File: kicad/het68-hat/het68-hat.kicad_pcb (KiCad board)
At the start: 2 copper layers, 94 x 96 mm, 91 parts, among them J1 MIC1, J10 PWR, J11 PZ1, J12 PZ2, J13 PZ3, J14 PZ4, J17 UART, J2 MIC2, J3 MIC3, J4 MIC4, J5 MIC5, J6 MIC6, U1 Pico_Plus_2, U2 SN74LVC8T245, U3 SN74LVC8T245, U4 SN74LVC8T245, U5 AP2112K-1.8, U6 DRV8837C, U7 DPS310, U8 SHT40, U9 INA3221

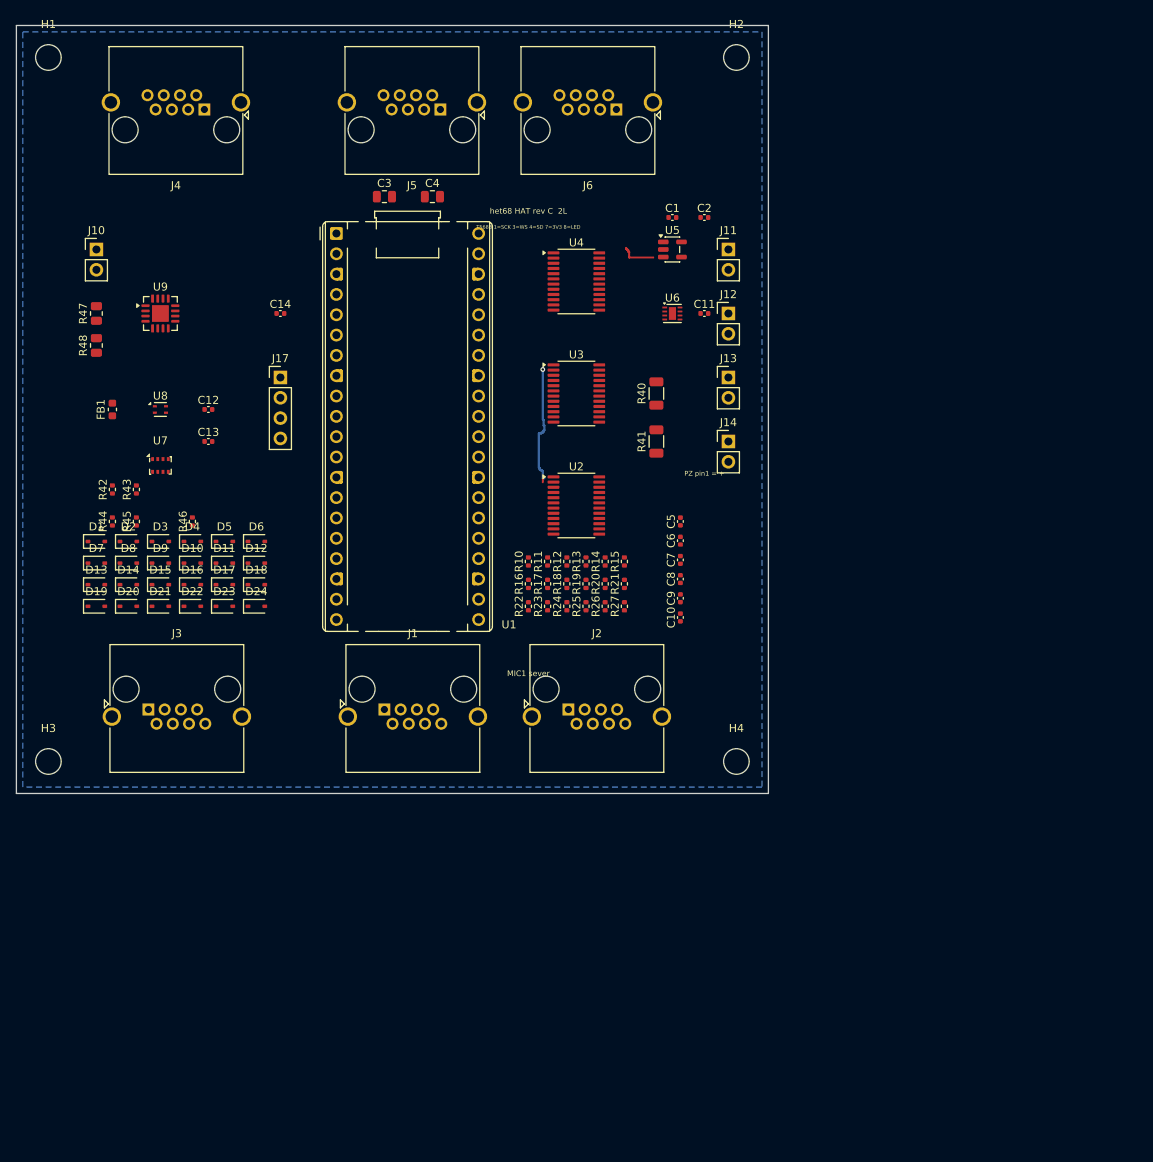
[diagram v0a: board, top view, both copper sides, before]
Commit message: Ship a four-layer HAT that is fully routed and ready to fab.
GPIO for SD and LED move to the jack rows so firmware can follow PINOUT.csv; power and satellite boards stay as in v1.10.0.

Co-authored-by: Cursor <cursoragent@cursor.com>
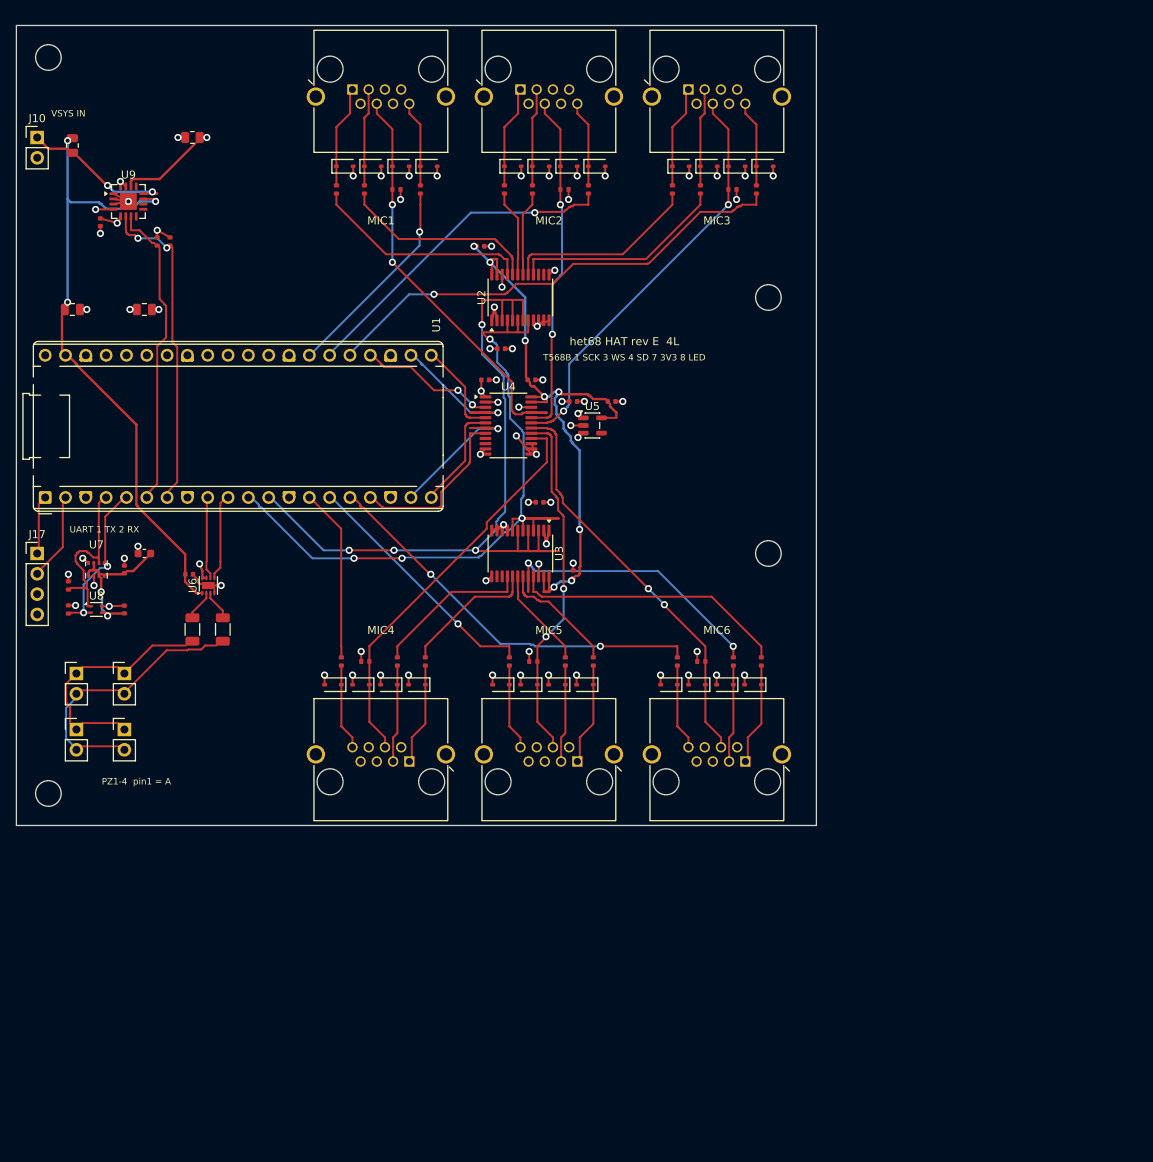
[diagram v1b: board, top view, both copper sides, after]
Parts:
- removed R46: 10k, R_0402_1005Metric
- added R50: 100k, Resistor_SMD:R_0402_1005Metric, F.Cu at (47.5, 20.5)
- added R51: 100k, Resistor_SMD:R_0402_1005Metric, F.Cu at (68.5, 20.5)
- added R52: 100k, Resistor_SMD:R_0402_1005Metric, F.Cu at (89.5, 20.5)
- added R53: 100k, Resistor_SMD:R_0402_1005Metric, F.Cu at (43.6, 79.5)
- added R54: 100k, Resistor_SMD:R_0402_1005Metric, F.Cu at (64.6, 79.5)
- added R55: 100k, Resistor_SMD:R_0402_1005Metric, F.Cu at (85.6, 79.5)
- C1, C10, C11, C12, C13, C14, C2, C5, C6, C7, C8, C9: footprint C_0402_1005Metric -> Capacitor_SMD:C_0402_1005Metric
- C3, C4: footprint C_0805_2012Metric -> Capacitor_SMD:C_0805_2012Metric
- D1, D10, D11, D12, D13, D14, D15, D16, D17, D18, D19, D2, D20, D21, D22, D23, D24, D3, D4, D5, D6, D7, D8, D9: footprint D_SOD-323 -> Diode_SMD:D_SOD-323
- FB1: footprint L_0603_1608Metric -> Inductor_SMD:L_0603_1608Metric
- H1, H2, H3, H4: footprint MountingHole_3.2mm_M3 -> MountingHole:MountingHole_3.2mm_M3
- J1, J2, J3, J4, J5, J6: footprint RJ45_Amphenol_RJHSE5380 -> het68:RJ45_RJHSE5380_het68
- J10, J11, J12, J13, J14: footprint PinHeader_1x02_P2.54mm_Vertical -> Connector_PinHeader_2.54mm:PinHeader_1x02_P2.54mm_Vertical
- J17: footprint PinHeader_1x04_P2.54mm_Vertical -> Connector_PinHeader_2.54mm:PinHeader_1x04_P2.54mm_Vertical
- R10, R11, R12, R13, R14, R15, R16, R17, R18, R19, R20, R21, R22, R23, R24, R25, R26, R27, R42, R43, R44, R45: footprint R_0402_1005Metric -> Resistor_SMD:R_0402_1005Metric
- R40, R41: footprint R_1206_3216Metric -> Resistor_SMD:R_1206_3216Metric
- R47, R48: footprint R_0805_2012Metric -> Resistor_SMD:R_0805_2012Metric
- U1: footprint RaspberryPi_Pico_Common_THT -> Module:RaspberryPi_Pico_Common_THT
- U2, U3, U4: footprint TSSOP-24_4.4x7.8mm_P0.65mm -> Package_SO:TSSOP-24_4.4x7.8mm_P0.65mm
- U5: footprint SOT-23-5 -> Package_TO_SOT_SMD:SOT-23-5
- U6: footprint Texas_DSG0008A_WSON-8-1EP_2x2mm_P0.5mm_EP0.9x1.6mm -> Package_SON:Texas_DSG0008A_WSON-8-1EP_2x2mm_P0.5mm_EP0.9x1.6mm
- U7: footprint Bosch_LGA-8_2x2.5mm_P0.65mm_ClockwisePinNumbering -> Package_LGA:Bosch_LGA-8_2x2.5mm_P0.65mm_ClockwisePinNumbering
- U8: footprint Sensirion_DFN-4_1.5x1.5mm_P0.8mm_SHT4x_NoCentralPad -> Sensor_Humidity:Sensirion_DFN-4_1.5x1.5mm_P0.8mm_SHT4x_NoCentralPad
- U9: footprint Texas_RGV0016A_VQFN-16-1EP_4x4mm_P0.65mm_EP2.1x2.1mm -> Package_DFN_QFN:Texas_RGV0016A_VQFN-16-1EP_4x4mm_P0.65mm_EP2.1x2.1mm
- moved H2 125.9 mm to (4.00, 96.0)
- moved H3 107.1 mm to (94.0, 34.0)
- moved J3 102.8 mm to (84.0, 8.00)
- moved J11 97.2 mm to (7.50, 81.0)
- moved J12 96.7 mm to (7.50, 88.0)
- moved J4 85.4 mm to (49.1, 92.0)
- moved J13 84.1 mm to (13.5, 81.0)
- moved J14 83.6 mm to (13.5, 88.0)
- moved J5 83.3 mm to (70.1, 92.0)
- moved J6 83.1 mm to (91.1, 92.0)
- moved D9 81.8 mm to (83.0, 17.6)
- moved D10 81.4 mm to (86.5, 17.6)
- moved D11 81.0 mm to (90.0, 17.6)
- moved D12 80.6 mm to (93.5, 17.6)
- moved J2 77.7 mm to (63.0, 8.00)
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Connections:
- U1 pad 14: LED1_G -> LED4_G
- U1 pad 15: LED2_G -> LED5_G
- U1 pad 16: LED3_G -> LED6_G
- U1 pad 17: LED4_G -> SD4_3V3
- U1 pad 19: LED5_G -> SD5_3V3
- U1 pad 20: (no net) -> SD6_3V3
- U1 pad 21: SD1_3V3 -> SD3_3V3
- U1 pad 22: (no net) -> SD2_3V3
- U1 pad 24: SD2_3V3 -> SD1_3V3
- U1 pad 25: (no net) -> LED3_G
- U1 pad 26: SD3_3V3 -> LED2_G
- U1 pad 27: (no net) -> LED1_G
- U1 pad 29: LED6_G -> unconnected-(U1-GP22-Pad29)
- U1 pad 30: RUN -> unconnected-(U1-RUN-Pad30)
- U1 pad 31: SD4_3V3 -> unconnected-(U1-GP26-Pad31)
- U1 pad 32: SD5_3V3 -> unconnected-(U1-GP27-Pad32)
- U1 pad 34: SD6_3V3 -> unconnected-(U1-GP28-Pad34)
- U1 pad 35: +3V3 -> unconnected-(U1-ADC_VREF-Pad35)
- U1 pad 37: (no net) -> unconnected-(U1-3V3_EN-Pad37)
- U1 pad 40: (no net) -> unconnected-(U1-VBUS-Pad40)
- U2 pad 14: (no net) -> unconnected-(U2-B8-Pad14)
- U2 pad 15: (no net) -> unconnected-(U2-B7-Pad15)
- U2 pad 16: SCK6_B -> WS3_B
- U2 pad 17: SCK5_B -> SCK3_B
- U2 pad 18: SCK4_B -> WS2_B
- U2 pad 19: SCK3_B -> SCK2_B
- U2 pad 20: SCK2_B -> WS1_B
- U2 pad 4: SCK_3V3 -> WS_3V3
- U2 pad 6: SCK_3V3 -> WS_3V3
- U2 pad 8: SCK_3V3 -> WS_3V3
- U3 pad 14: (no net) -> unconnected-(U3-B8-Pad14)
- U3 pad 15: (no net) -> unconnected-(U3-B7-Pad15)
- U3 pad 16: WS6_B -> WS4_B
- U3 pad 17: WS5_B -> SCK4_B
- U3 pad 18: WS4_B -> WS5_B
- U3 pad 19: WS3_B -> SCK5_B
- U3 pad 20: WS2_B -> WS6_B
- U3 pad 21: WS1_B -> SCK6_B
- U3 pad 3: WS_3V3 -> SCK_3V3
- U3 pad 5: WS_3V3 -> SCK_3V3
- U3 pad 7: WS_3V3 -> SCK_3V3
- U4 pad 10: (no net) -> unconnected-(U4-A8-Pad10)
- U4 pad 16: SD6_18 -> SD4_18
- U4 pad 18: SD4_18 -> SD6_18
- U4 pad 6: SD4_3V3 -> SD6_3V3
- U4 pad 8: SD6_3V3 -> SD4_3V3
- U4 pad 9: (no net) -> unconnected-(U4-A7-Pad9)
- U5 pad 4: (no net) -> unconnected-(U5-NC-Pad4)
- U9 pad 10: (no net) -> unconnected-(U9-PV-Pad10)
- U9 pad 13: (no net) -> unconnected-(U9-TC-Pad13)
- U9 pad 8: (no net) -> unconnected-(U9-WARNING-Pad8)
- U9 pad 9: (no net) -> unconnected-(U9-CRITICAL-Pad9)
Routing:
- net SCK_3V3: track 0.00 -> 98.5 mm, vias 0 -> 4
- net WS_3V3: track 0.00 -> 90.1 mm, vias 0 -> 4
- net GND: track 0.00 -> 89.3 mm, vias 0 -> 59
- net +1V8: track 0.00 -> 79.0 mm, vias 0 -> 8
- net VSYS: track 0.00 -> 77.2 mm, vias 0 -> 3
- net LED3_G: track 0.00 -> 60.0 mm, vias 0 -> 1
- net SD3_18: track 0.00 -> 52.4 mm, vias 0 -> 2
- net SD1_18: track 0.00 -> 52.1 mm, vias 0 -> 2
- net SD6_18: track 0.00 -> 51.2 mm, vias 0 -> 2
- net SD4_18: track 0.00 -> 50.6 mm
- net LED6_G: track 0.00 -> 49.9 mm, vias 0 -> 2
- net SD5_18: track 0.00 -> 44.4 mm, vias 0 -> 2
- net SD2_18: track 0.00 -> 43.0 mm, vias 0 -> 2
- net LED2_G: track 0.00 -> 41.5 mm, vias 0 -> 1
- net I2C0_SCL: track 0.00 -> 40.2 mm, vias 0 -> 2
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- added copper zone on In2.Cu, net +3V3
- added copper zone on In2.Cu, net +3V3_MIC
- added copper zone on In1.Cu, net GND
- removed copper zone on B.Cu, net GND
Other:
- board size 94 x 96 mm -> 100 x 100 mm
- copper layers 2 -> 4
- board text added: "MIC1"
- board text added: "MIC2"
- board text added: "MIC3"
- board text added: "MIC4"
- board text added: "MIC5"
- board text added: "MIC6"
- board text added: "PZ1-4 pin1 = A"
- board text added: "T568B 1 SCK 3 WS 4 SD 7 3V3 8 LED"
- board text added: "UART 1 TX 2 RX"
- board text added: "VSYS IN"
- board text added: "het68 HAT rev E 4L"
- board text removed: "MIC1 sever"
- board text removed: "PZ pin1 = +"
- board text removed: "T568B 1=SCK 3=WS 4=SD 7=3V3 8=LED"
- board text removed: "het68 HAT rev C 2L"

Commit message: Fit every board on printed.cz prototype: 2-layer, 0603, ENIG.
HAT is 140×140 mm so it routes on two layers without 0402 or BGA; satellite and power use the same stack, drill and finish.

Co-authored-by: Cursor <cursoragent@cursor.com>
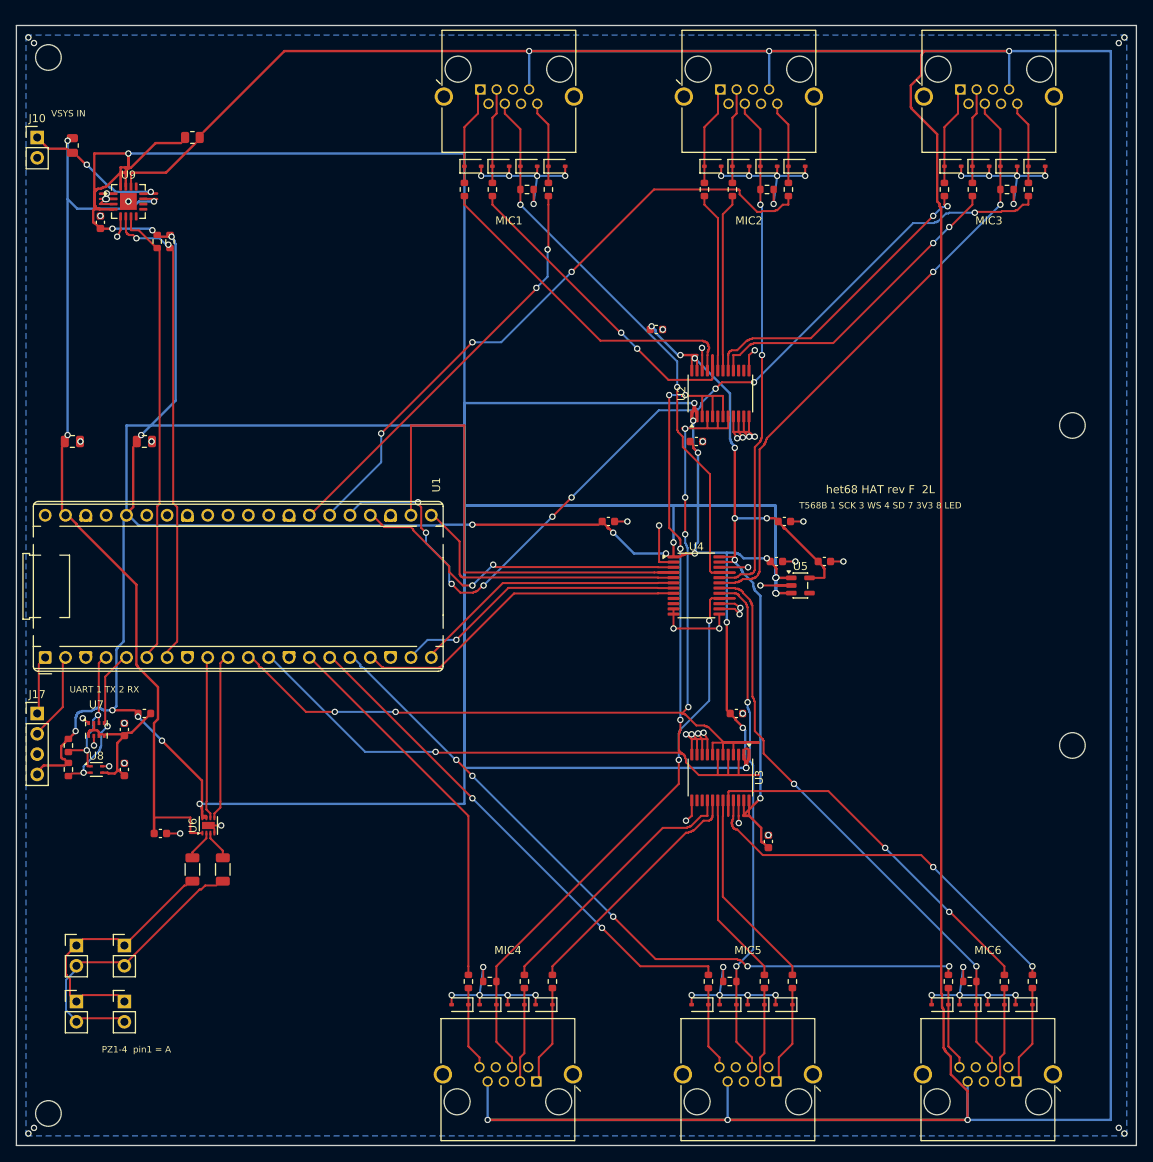
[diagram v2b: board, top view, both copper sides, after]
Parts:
- C1, C10, C11, C12, C13, C14, C2, C5, C6, C7, C8, C9: footprint Capacitor_SMD:C_0402_1005Metric -> Capacitor_SMD:C_0603_1608Metric
- R10, R11, R12, R13, R14, R15, R16, R17, R18, R19, R20, R21, R22, R23, R24, R25, R26, R27, R42, R43, R44, R45, R50, R51, R52, R53, R54, R55: footprint Resistor_SMD:R_0402_1005Metric -> Resistor_SMD:R_0603_1608Metric
- moved D21 52.4 mm to (126.0, 122.4)
- moved D22 52.4 mm to (122.5, 122.4)
- moved D23 52.4 mm to (119.0, 122.4)
- moved D24 52.4 mm to (115.5, 122.4)
- moved J6 52.4 mm to (125.0, 132.0)
- moved R25 52.4 mm to (127.0, 119.5)
- moved R26 52.4 mm to (123.5, 119.5)
- moved R27 52.4 mm to (116.5, 119.5)
- moved R55 52.2 mm to (119.2, 119.5)
- moved D17 47.1 mm to (96.0, 122.4)
- moved D18 47.1 mm to (92.5, 122.4)
- moved D19 47.1 mm to (89.0, 122.4)
- moved D20 47.1 mm to (85.5, 122.4)
- moved R24 47.1 mm to (86.5, 119.5)
- moved J5 47.1 mm to (95.0, 132.0)
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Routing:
- net +3V3: track 27.7 -> 783.2 mm, vias 18 -> 27
- net +3V3_MIC: track 11.6 -> 627.0 mm, vias 1 -> 6
- net GND: track 89.3 -> 217.0 mm, vias 59 -> 80
- net LED3_G: track 60.0 -> 115.1 mm, vias 1 -> 9
- net SD2_3V3: track 19.2 -> 64.3 mm, vias 1 -> 0
- net SCK_3V3: track 98.5 -> 141.3 mm, vias 4 -> 5
- net LED6_G: track 49.9 -> 92.0 mm, vias 2 -> 5
- net LED2_G: track 41.5 -> 79.2 mm, vias 1 -> 3
- net VSYS: track 77.2 -> 114.6 mm
- net WS_3V3: track 90.1 -> 125.1 mm, vias 4 -> 6
- net LED5_G: track 31.4 -> 64.2 mm, vias 1 -> 2
- net LED1_G: track 25.8 -> 52.2 mm, vias 1 -> 2
- net LED4_G: track 21.5 -> 47.8 mm
- net SD1_3V3: track 17.6 -> 43.1 mm
- net SD3_18: track 52.4 -> 77.5 mm
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- added copper zone on B.Cu, net GND
- removed copper zone on In2.Cu, net +3V3
- removed copper zone on In2.Cu, net +3V3_MIC
- removed copper zone on In1.Cu, net GND
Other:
- board size 100 x 100 mm -> 140 x 140 mm
- copper layers 4 -> 2
- board text added: "het68 HAT rev F 2L"
- board text removed: "het68 HAT rev E 4L"
